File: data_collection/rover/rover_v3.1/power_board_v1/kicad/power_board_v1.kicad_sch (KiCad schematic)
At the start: 96 parts, among them J1 XT60_BATT, J10 from Pi USB2, J11 UPDI prog (UPDI/3V3/GND), J12 XT30 fallback pads, J2 PANEL_SW, J3 USB4105-GF-A (TH shell), J4 USB_A radio1, J5 USB_A radio2, J6 AUX 5V 2A, J7 PI GPIO harness, J8 AUX_CTL out (JST-GH), J9 from Pi USB1, Q2 CSD18543Q3A diode, Q3 CSD18543Q3A switch, U1 LM5145 5.1V rail A, U2 LM5145 5.1V rail B, U3 ATtiny816 (VQFN), U4 LM74800-Q1, U5 INA226 (addr 0x40), U6 TPS7A1633 3V3 60V LDO, U7 TPS2553 1.7A, U8 TPS2553 1.7A, U9 AP2112K-3.3 (switched)

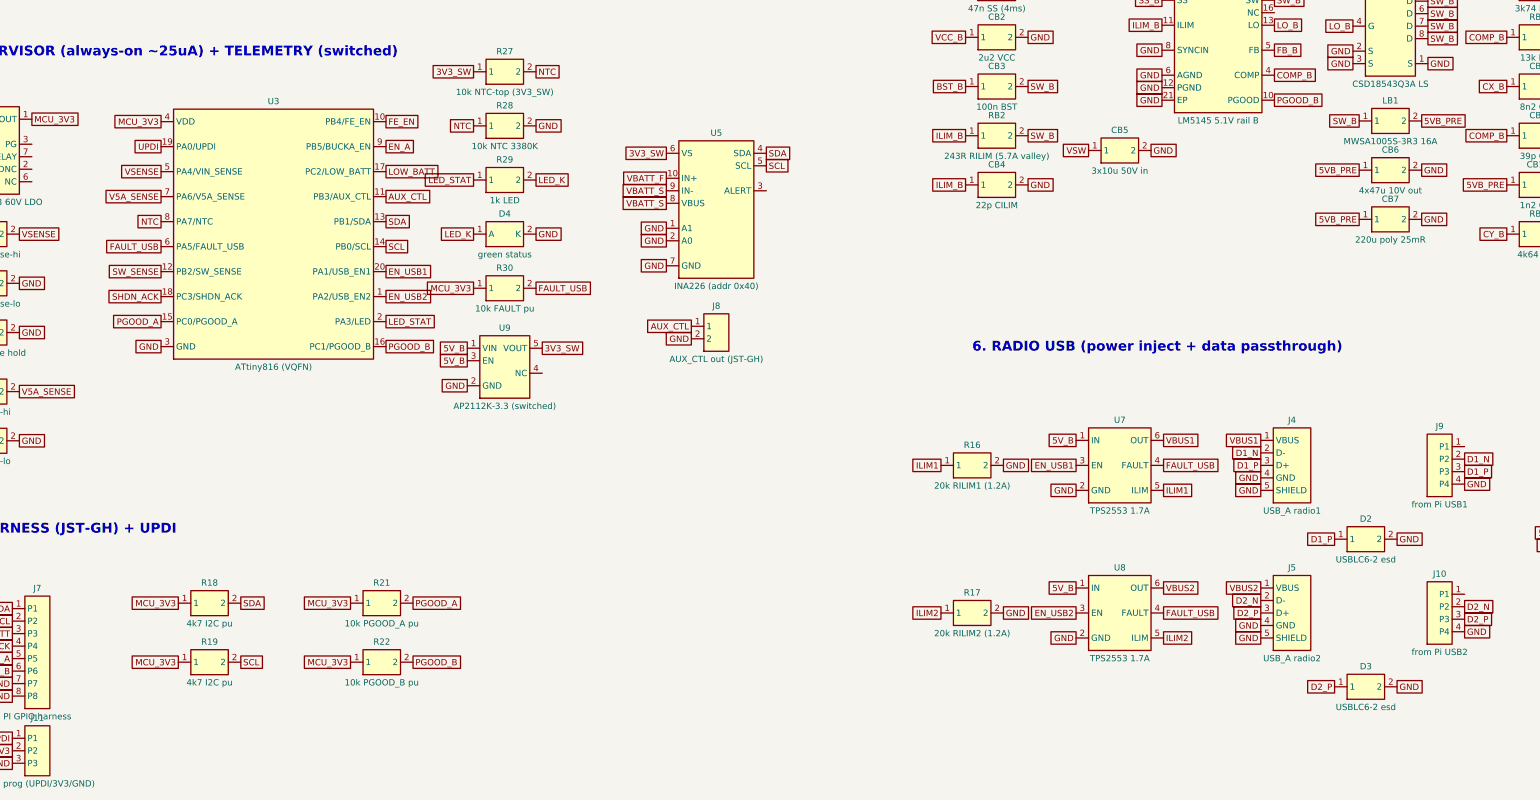
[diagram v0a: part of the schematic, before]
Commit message: P4 start: generate_board.py -> 90x65 board, 96 placed footprints, full net binding; board-gen audit fixed USBLC6 (was 2-pin, D-/VBUS unprotected) + ATtiny EP grounding; schematic v3 regenerated
Co-Authored-By: Claude Fable 5 <noreply@anthropic.com>
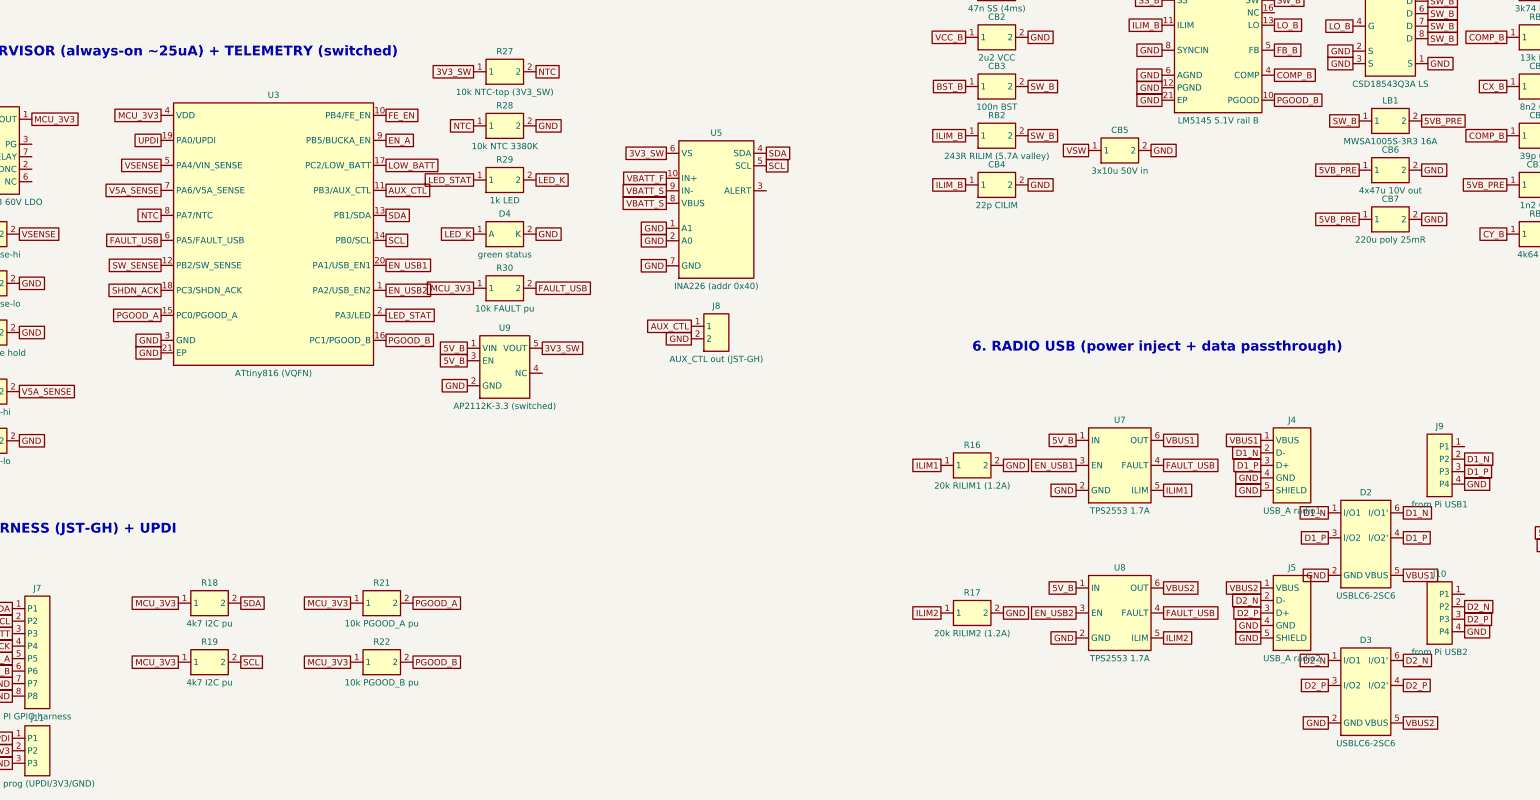
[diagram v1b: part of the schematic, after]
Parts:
- removed D2, D3: USBLC6-2 esd, Package_TO_SOT_SMD:SOT-23-6, symbol pwr:TVS
- added D2, D3: USBLC6-2SC6, Package_TO_SOT_SMD:SOT-23-6, symbol pwr:USBLC6
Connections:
- net D1_N: now also D2.1 (I/O1), D2.6 (I/O1')
- net D1_P: now also D2.3 (I/O2), D2.4 (I/O2')
- net D2_N: now also D3.1 (I/O1), D3.6 (I/O1')
- net D2_P: now also D3.3 (I/O2), D3.4 (I/O2')
- net GND: now also U3.21 (EP), D2.2 (GND), D3.2 (GND)
- net VBUS1: now also D2.5 (VBUS)
- net VBUS2: now also D3.5 (VBUS)

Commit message: Adversarial review response: schematic v4 (decoupling C5-C17+CE1, split bulk caps ->127 comps, 3V3_SW pulls, PGOOD seq divider fixes INA226 abs-max + bootstrap deadlock, rail-A sense/setpoint, wc RILIM, aux polyfuse, 5V TVS, rev-batt schottky, FE_EN delay); firmware boot-glitch + cold-on fixes (11 tests green); board re-floorplan (J1/J12/J3 orientations, monotonic power corridor, tight hot loops, refill-after-resolve, solid pours + 20 thermal vias); REVIEW_FINDINGS.md disposition
Co-Authored-By: Claude Fable 5 <noreply@anthropic.com>
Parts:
- removed CA11, CB11: 2x22u pi-out, Capacitor_SMD:C_1206_3216Metric, symbol pwr:CAP
- removed CA5, CB5: 3x10u 50V in, Capacitor_SMD:C_1210_3225Metric, symbol pwr:CAP
- removed CA6, CB6: 4x47u 10V out, Capacitor_SMD:C_1210_3225Metric, symbol pwr:CAP
- removed L2: pi-filter 1u, Inductor_SMD:L_Chilisin_BMRx00060630, symbol pwr:IND
- added C10: 100n INA vs, Capacitor_SMD:C_0402_1005Metric, symbol pwr:CAP
- added C13: 100n U7 in, Capacitor_SMD:C_0402_1005Metric, symbol pwr:CAP
- added C14: 100n U8 in, Capacitor_SMD:C_0402_1005Metric, symbol pwr:CAP
- added C15: 100n at U4.A, Capacitor_SMD:C_0402_1005Metric, symbol pwr:CAP
- added C16: 2u2 EN delay, Capacitor_SMD:C_0603_1608Metric, symbol pwr:CAP
- added C17: 100n sw debounce, Capacitor_SMD:C_0402_1005Metric, symbol pwr:CAP
- added C5: 1u LDO in, Capacitor_SMD:C_0603_1608Metric, symbol pwr:CAP
- added C6: 100n LDO in, Capacitor_SMD:C_0402_1005Metric, symbol pwr:CAP
- added C7: 2u2 LDO out, Capacitor_SMD:C_0603_1608Metric, symbol pwr:CAP
- added C8: 100n MCU vdd, Capacitor_SMD:C_0402_1005Metric, symbol pwr:CAP
- added C9: 1u LDO out, Capacitor_SMD:C_0603_1608Metric, symbol pwr:CAP
- added CA111, CA112: 22u local, Capacitor_SMD:C_1206_3216Metric, symbol pwr:CAP
- added CA51, CA52, CA53, CB51, CB52, CB53: 10u 50V X7R, Capacitor_SMD:C_1210_3225Metric, symbol pwr:CAP
- added CA61, CA62, CA63, CA64, CB61, CB62, CB63, CB64: 47u 10V X7R, Capacitor_SMD:C_1210_3225Metric, symbol pwr:CAP
- added CB111, CB112: 22u pi-out, Capacitor_SMD:C_1206_3216Metric, symbol pwr:CAP
- added CE1: 100u hybrid 25V, Capacitor_SMD:CP_Elec_8x10, symbol pwr:CAP
- added D5: B5819W schottky, Diode_SMD:D_SOD-123, symbol pwr:TVS
- added D6, D7: SMBJ5.0A, Diode_SMD:D_SMB, symbol pwr:TVS
- added F2: 2A polyfuse, Fuse:Fuse_1812_4532Metric, symbol pwr:FUSE
- added R31: 100k EN1 pu (5V_B), Resistor_SMD:R_0402_1005Metric, symbol pwr:RES
- added R32: 100k EN2 pu (5V_B), Resistor_SMD:R_0402_1005Metric, symbol pwr:RES
- added R33: 20k seq div hi, Resistor_SMD:R_0402_1005Metric, symbol pwr:RES
- added R34: 16k5 seq div lo, Resistor_SMD:R_0402_1005Metric, symbol pwr:RES
- R18, R19: value 4k7 I2C pu -> 4k7 I2C pu (3V3_SW)
- R21: value 10k PGOOD_A pu -> 20k PGOOD_A pu (5V_A)
- R22: value 10k PGOOD_B pu -> 10k PGOOD_B pu (3V3_SW)
- RA2: value 301R RILIM (7A valley) -> 348R RILIM (wc-min 6.3A)
- RA4: value 3k74 RFB2 -> 3k65 RFB2 (5.18V)
- RB2: value 243R RILIM (5.7A valley) -> 261R RILIM (wc-min 4.8A)
- RB4: value 3k74 RFB2 -> 3k74 RFB2 (5.08V)
- U1: value LM5145 5.1V rail A -> LM5145 rail A
- U2: value LM5145 5.1V rail B -> LM5145 rail B
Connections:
- net 5VA_PRE is gone; now on net 5V_A: CA10.1, CA7.1, LA1.2, RA3.1
- net 3V3_SW: now also R18.1, R19.1, R22.1, C10.1, C9.1
- net 5VB_PRE: now also CB61.1, CB62.1, CB63.1, CB64.1
- net 5V_A: now also R21.1, CA111.1, CA112.1, CA61.1, CA62.1, CA63.1, CA64.1, D6.1
- net 5V_B: now also C13.1, C14.1, CB111.1, CB112.1, D7.1, F2.1, R31.1, R32.1; no longer J6.1
- net EN_USB1: now also R31.2
- net EN_USB2: now also R32.2
- net FE_EN: now also C16.1
- net GND: now also C10.2, C13.2, C14.2, C15.2, C16.2, C17.2, C5.2, C6.2, C7.2, C8.2, C9.2, CA111.2, CA112.2, CA51.2, CA52.2, CA53.2, CA61.2, CA62.2, CA63.2, CA64.2, CB111.2, CB112.2, CB51.2, CB52.2, CB53.2, CB61.2, CB62.2, CB63.2, CB64.2, CE1.2, D6.2, D7.2, R34.2
- net MCU_3V3: now also C7.1, C8.1; no longer R18.1, R19.1, R21.1, R22.1
- net PGOOD_A: now also R33.2, R34.1; no longer R21.2, U1.10 (PGOOD)
- net SW_SENSE: now also C17.1
- net VBATT_F: now also D5.1; no longer U6.5 (EN), U6.8 (IN)
- net VBATT_S: now also C15.1
- net VSW: now also CA51.1, CA52.1, CA53.1, CB51.1, CB52.1, CB53.1, CE1.1
- new net AUX_5V: F2.2, J6.1
- new net PGOODA_RAW: R21.2, R33.1, U1.10 (PGOOD)
- new net VBATT_FD: C5.1, C6.1, D5.2, U6.5 (EN), U6.8 (IN)
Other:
- note added: "4. BUCK A 5.18V/6A (Pi 5) [values: P1_DETAIL_DESIGN.md sec 2]"
- note added: "5. BUCK B 5.08V/5A (radios+aux) — EN = PGOOD_A (Pi rail first)"
- note removed: "4. BUCK A 5.1V/6A (Pi 5) [values: P1_DETAIL_DESIGN.md sec 2]"
- note removed: "5. BUCK B 5.1V/5A (radios+aux) — EN = PGOOD_A (Pi rail first)"
